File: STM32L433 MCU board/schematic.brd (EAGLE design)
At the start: 55 x 60 mm, 28 parts, among them T1 2N2222, U2 STM32L476RCT6, Y2 ABS25-32.768KHZ-6-T, Y3 ECS-160-S-5PX-TR

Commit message: Added gitignore
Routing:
- net 3.3V: track 157.0 -> 0.00 mm, vias 6 -> 0
- net TX1: track 80.5 -> 0.00 mm, vias 1 -> 0
- net CS5: track 77.1 -> 0.00 mm
- net IGN3_2: track 67.0 -> 0.00 mm, vias 2 -> 0
- net IGN3_1: track 64.6 -> 0.00 mm, vias 1 -> 0
- net IGN_CHK3: track 62.6 -> 0.00 mm, vias 4 -> 0
- net CS4: track 62.3 -> 0.00 mm, vias 2 -> 0
- net STAT_LED: track 61.8 -> 0.00 mm, vias 2 -> 0
- net LIPO: track 59.4 -> 0.00 mm, vias 2 -> 0
- net IGN1_1: track 56.8 -> 0.00 mm, vias 1 -> 0
- net SD_CS: track 56.6 -> 0.00 mm, vias 6 -> 0
- net BUZZ: track 56.4 -> 0.00 mm, vias 4 -> 0
- net SPI1_MOSI: track 56.1 -> 0.00 mm, vias 8 -> 0
- net CS2: track 53.4 -> 0.00 mm
- net SPI1_SCK: track 52.3 -> 0.00 mm, vias 4 -> 0
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
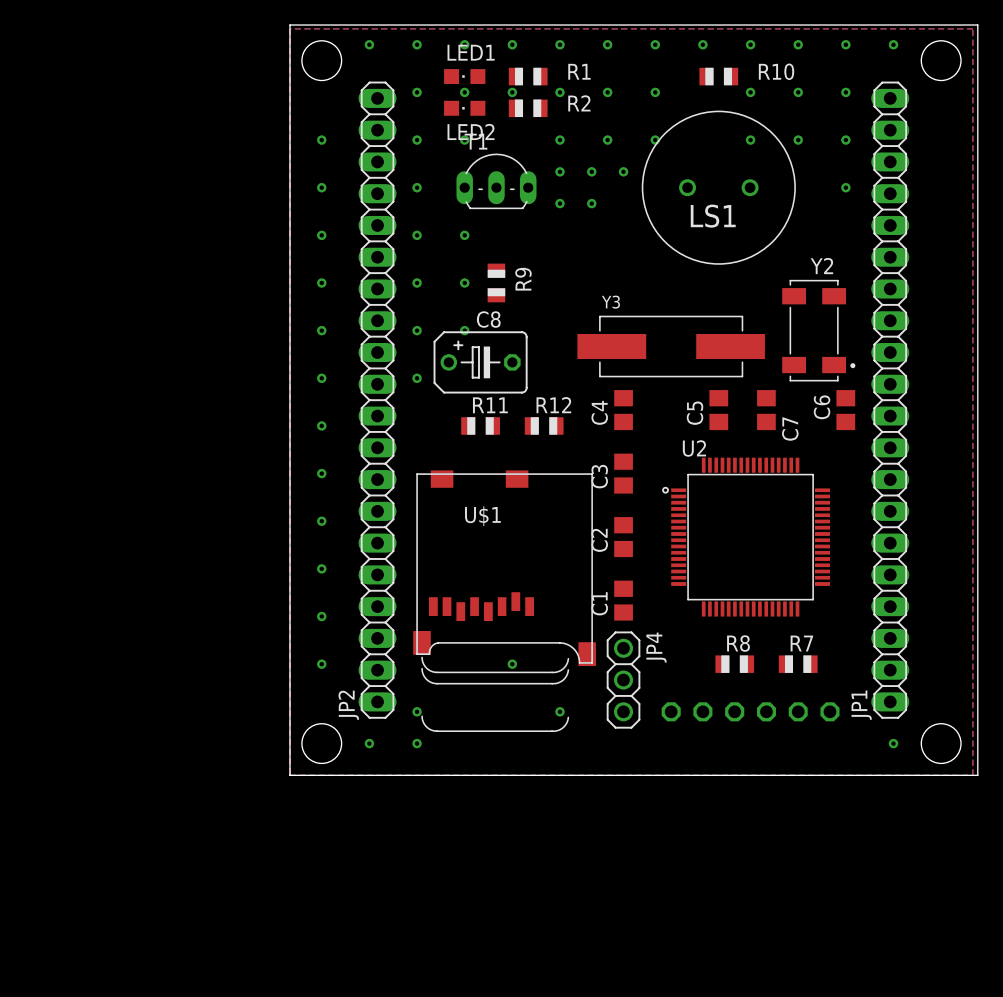
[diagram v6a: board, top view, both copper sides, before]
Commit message: Finished routing and ground plane stitching
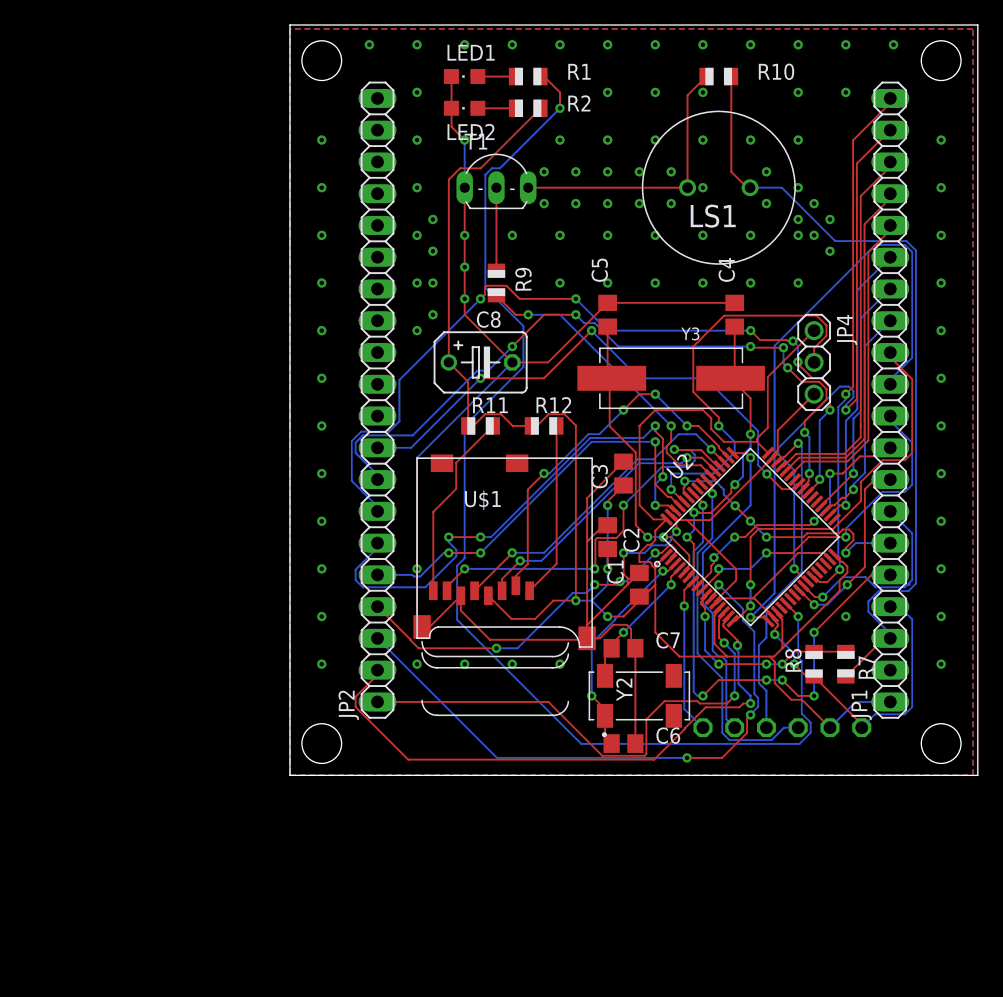
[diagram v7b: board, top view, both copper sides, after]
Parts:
- moved Y2 32.4 mm to (27.9, 6.35), turned to 90 degrees
- moved C6 32.1 mm to (26.7, 2.54), turned to 0 degrees
- moved JP4 29.6 mm to (41.9, 33.0)
- moved C7 22.2 mm to (26.7, 10.2), turned to 0 degrees
- moved C4 11.7 mm to (35.6, 36.8)
- moved C5 11.7 mm to (25.4, 36.8)
- moved R8 6.35 mm to (41.9, 8.89), turned to 90 degrees
- moved R7 3.81 mm to (44.5, 8.89), turned to 270 degrees
- moved JP3 2.84 mm to (39.4, 3.81)
- moved Y3 2.54 mm to (30.5, 31.8)
- moved C1 1.80 mm to (27.9, 15.2)
- moved C2 1.27 mm to (25.4, 19.1)
- moved U$1 1.27 mm to (10.2, 25.4)
- turned U2 to 45 degrees
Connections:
- net BUZZ: now also U2.54; no longer U2.28
- net IGN1_1: now also U2.14; no longer U2.56
- net IGN1_2: now also U2.15; no longer U2.57
- net IGN2_1: now also U2.11; no longer U2.61
- net IGN2_2: now also U2.2; no longer U2.62
- net IGN3_1: now also U2.61; no longer U2.29
- net IGN3_2: now also U2.62; no longer U2.30
- net IGN_CHK1: now also U2.39; no longer U2.22
- net IGN_CHK2: now also U2.40; no longer U2.23
- net RX1: now also U2.25; no longer U2.24
- net SD_CS: now also U2.50; no longer U2.42
- net TX1: now also U2.24; no longer U2.25
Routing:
- net GND: track 0.00 -> 197.3 mm, vias 0 -> 91
- net 3.3V: track 0.00 -> 170.5 mm, vias 0 -> 4
- net STAT_LED: track 0.00 -> 94.5 mm, vias 0 -> 2
- net IGN_CHK1: track 0.00 -> 65.5 mm, vias 0 -> 7
- net LIPO: track 0.00 -> 64.5 mm
- net IGN_CHK2: track 0.00 -> 57.8 mm, vias 0 -> 7
- net RX3: track 0.00 -> 49.9 mm, vias 0 -> 1
- net IGN2_1: track 0.00 -> 49.3 mm, vias 0 -> 3
- net IGN1_2: track 0.00 -> 46.9 mm, vias 0 -> 2
- net CS4: track 0.00 -> 45.5 mm, vias 0 -> 2
- net IGN_CHK3: track 0.00 -> 44.6 mm, vias 0 -> 3
- net IGN3_2: track 0.00 -> 43.6 mm, vias 0 -> 5
- net CS5: track 0.00 -> 42.2 mm, vias 0 -> 2
- net IGN1_1: track 0.00 -> 41.5 mm, vias 0 -> 2
- net SCL0: track 0.00 -> 40.4 mm, vias 0 -> 6
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
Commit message: Update schematic.brd
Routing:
- net GND: vias 91 -> 125
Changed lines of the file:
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@@
 <drawing>
 <settings>
-<setting alwaysvectorfont="yes"/>
+<setting alwaysvectorfont="no"/>
 <setting verticaltext="up"/>
 </settings>
@@
 <wire x1="41.45689375" y1="7.755" x2="42.045" y2="7.755" width="0.1524" layer="1"/>
 <wire x1="17.78" y1="33.02" x2="10.16" y2="25.4" width="0.1524" layer="16"/>
-<wire x1="10.16" y1="25.4" x2="10.16" y2="16.51" width="0.1524" layer="16"/>
+<wire x1="10.16" y1="25.4" x2="10.16" y2="24.13" width="0.1524" layer="16"/>
 <via x="10.16" y="16.51" extent="1-16" drill="0.35"/>
+<wire x1="10.16" y1="24.13" x2="10.16" y2="20.32" width="0.1524" layer="16"/>
+<wire x1="10.16" y1="20.32" x2="10.16" y2="16.51" width="0.1524" layer="16"/>
 <wire x1="10.16" y1="16.51" x2="10.16" y2="12.26" width="0.1524" layer="1"/>
 <wire x1="10.16" y1="12.26" x2="10.56" y2="11.86" width="0.1524" layer="1"/>
@@
 <via x="36.83" y="39.37" extent="1-16" drill="0.35"/>
 <via x="40.64" y="39.37" extent="1-16" drill="0.35"/>
-<via x="40.64" y="43.18" extent="1-16" drill="0.35"/>
 <via x="40.64" y="46.99" extent="1-16" drill="0.35"/>
 <via x="40.64" y="50.8" extent="1-16" drill="0.35"/>
@@
 <via x="13.97" y="40.64" extent="1-16" drill="0.35"/>
 <via x="13.97" y="43.18" extent="1-16" drill="0.35"/>
+<via x="38.1" y="45.72" extent="1-16" drill="0.35"/>
+<via x="40.64" y="44.45" extent="1-16" drill="0.35"/>
+<via x="41.91" y="43.18" extent="1-16" drill="0.35"/>
+<via x="43.18" y="41.91" extent="1-16" drill="0.35"/>
+<via x="43.18" y="44.45" extent="1-16" drill="0.35"/>
+<via x="41.91" y="45.72" extent="1-16" drill="0.35"/>
+<via x="38.1" y="48.26" extent="1-16" drill="0.35"/>
+<via x="10.16" y="24.13" extent="1-16" drill="0.35"/>
+<via x="10.16" y="20.32" extent="1-16" drill="0.35"/>
+<via x="11.43" y="44.45" extent="1-16" drill="0.35"/>
+<via x="11.43" y="41.91" extent="1-16" drill="0.35"/>
+<via x="11.43" y="39.37" extent="1-16" drill="0.35"/>
+<via x="11.43" y="36.83" extent="1-16" drill="0.35"/>
+<via x="27.94" y="36.83" extent="1-16" drill="0.35"/>
+<via x="31.75" y="36.83" extent="1-16" drill="0.35"/>
+<via x="29.21" y="33.02" extent="1-16" drill="0.35"/>
+<via x="39.37" y="38.1" extent="1-16" drill="0.35"/>
+<via x="39.37" y="40.64" extent="1-16" drill="0.35"/>
+<via x="41.91" y="40.64" extent="1-16" drill="0.35"/>
+<via x="43.18" y="48.26" extent="1-16" drill="0.35"/>
+<via x="43.18" y="50.8" extent="1-16" drill="0.35"/>
+<via x="45.72" y="53.34" extent="1-16" drill="0.35"/>
+<via x="12.7" y="26.67" extent="1-16" drill="0.35"/>
+<via x="11.43" y="22.86" extent="1-16" drill="0.35"/>
+<via x="12.7" y="11.43" extent="1-16" drill="0.35"/>
+<via x="12.7" y="7.62" extent="1-16" drill="0.35"/>
+<via x="16.51" y="7.62" extent="1-16" drill="0.35"/>
+<via x="20.32" y="7.62" extent="1-16" drill="0.35"/>
+<via x="22.86" y="7.62" extent="1-16" drill="0.35"/>
+<via x="21.59" y="8.89" extent="1-16" drill="0.35"/>
+<via x="20.32" y="10.16" extent="1-16" drill="0.35"/>
+<via x="22.86" y="5.08" extent="1-16" drill="0.35"/>
+<via x="26.67" y="5.08" extent="1-16" drill="0.35"/>
+<via x="26.67" y="7.62" extent="1-16" drill="0.35"/>
+<via x="29.21" y="7.62" extent="1-16" drill="0.35"/>
 </signal>
 <signal name="3.3V" class="1">
@@
 <wire x1="25.19" y1="5.29" x2="25.19" y2="4.75" width="0.1524" layer="1"/>
 </signal>
-<signal name="N$89">
-<via x="21.59" y="8.89" extent="1-16" drill="0.35"/>
-</signal>
-<signal name="N$9">
-<via x="38.1" y="45.72" extent="1-16" drill="0.35"/>
-</signal>
-<signal name="N$10">
-<via x="38.1" y="48.26" extent="1-16" drill="0.35"/>
-</signal>
-<signal name="N$13">
-<via x="40.64" y="44.45" extent="1-16" drill="0.35"/>
-</signal>
-<signal name="N$14">
-<via x="41.91" y="45.72" extent="1-16" drill="0.35"/>
-</signal>
 <signal name="N$15">
-<via x="41.91" y="43.18" extent="1-16" drill="0.35"/>
-</signal>
-<signal name="N$16">
-<via x="43.18" y="44.45" extent="1-16" drill="0.35"/>
-</signal>
-<signal name="N$17">
-<via x="43.18" y="41.91" extent="1-16" drill="0.35"/>
-</signal>
-<signal name="N$18">
-<via x="11.43" y="36.83" extent="1-16" drill="0.35"/>
-</signal>
-<signal name="N$19">
-<via x="11.43" y="39.37" extent="1-16" drill="0.35"/>
-</signal>
-<signal name="N$20">
-<via x="11.43" y="41.91" extent="1-16" drill="0.35"/>
-</signal>
-<signal name="N$21">
-<via x="11.43" y="44.45" extent="1-16" drill="0.35"/>
+<via x="45.72" y="11.43" extent="1-16" drill="0.35"/>
 </signal>
 </signals>
